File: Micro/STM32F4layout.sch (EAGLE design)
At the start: 38 parts, among them Q1 ASF, U1 LM1085IS-3.3

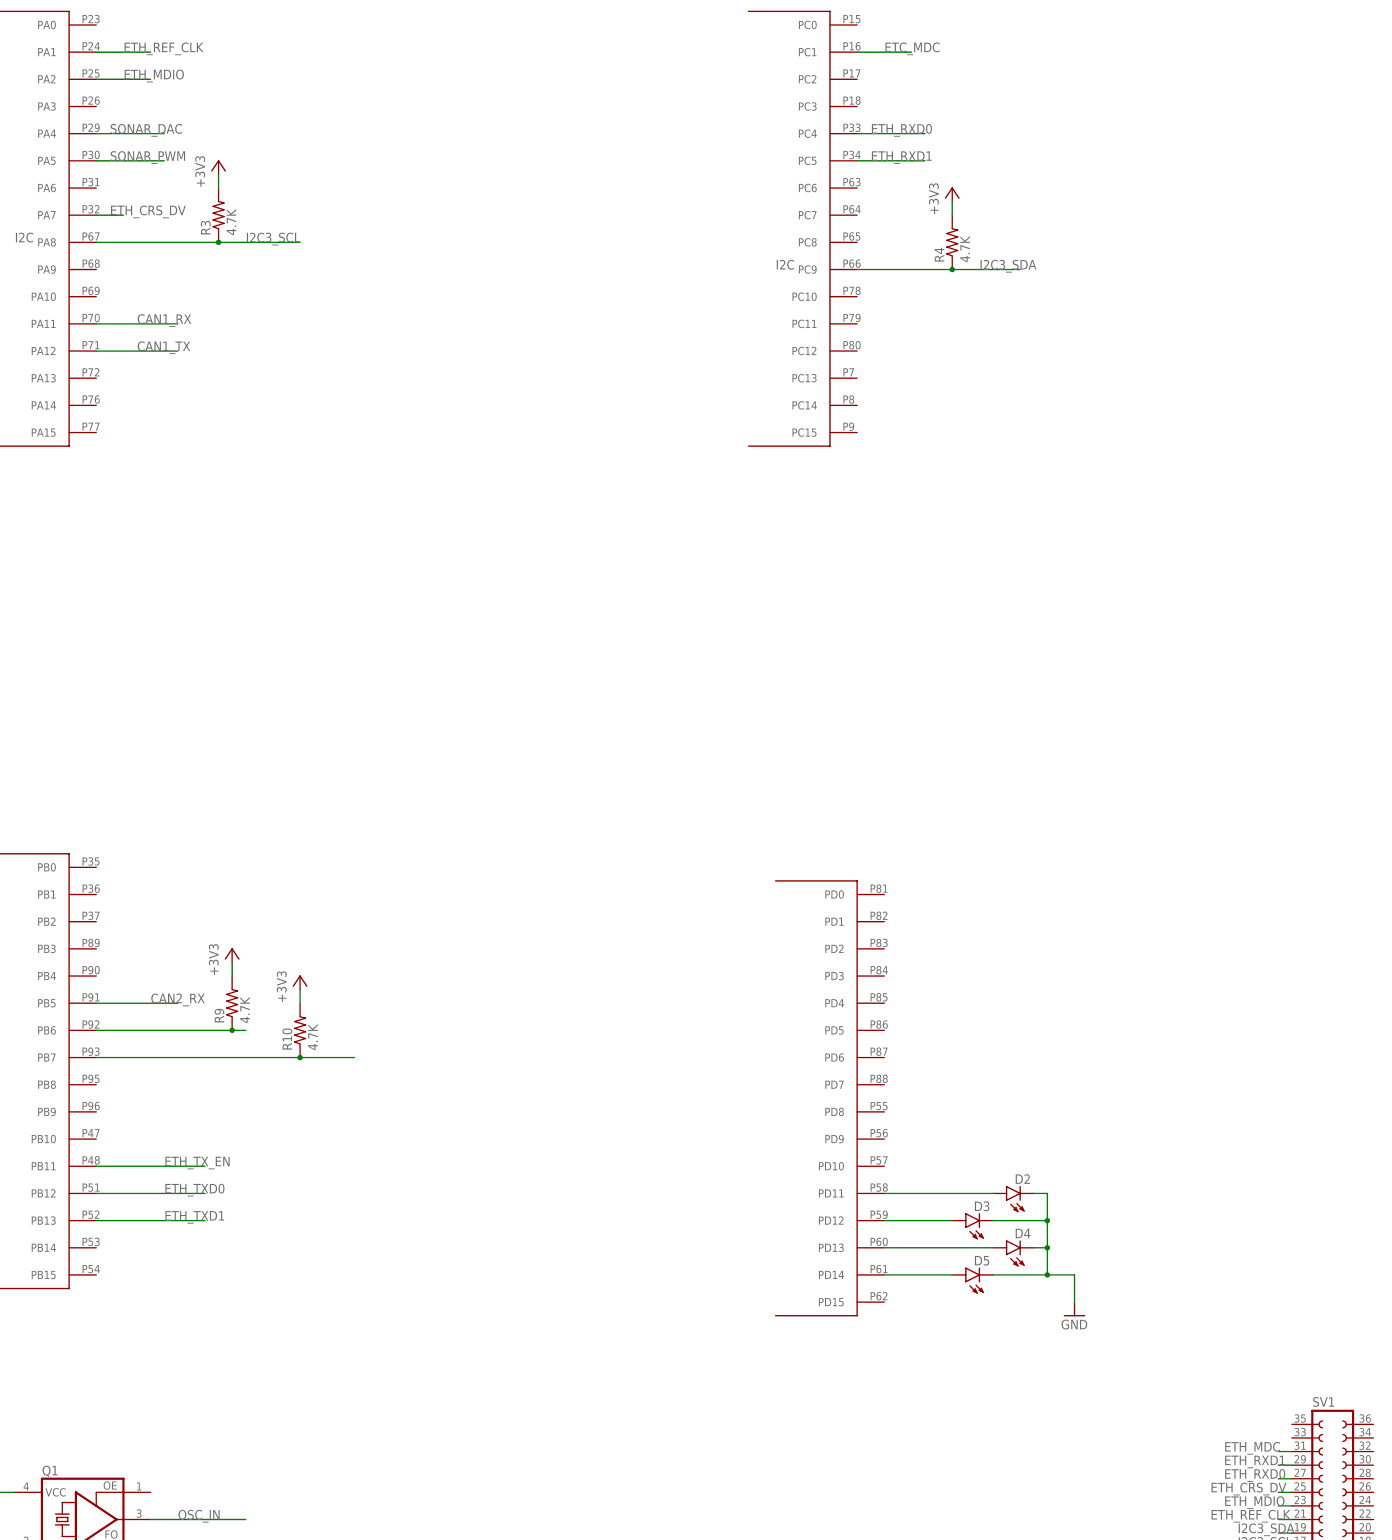
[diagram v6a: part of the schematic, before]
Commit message: Final Version before Design Review
Fixed Pin Out Problems
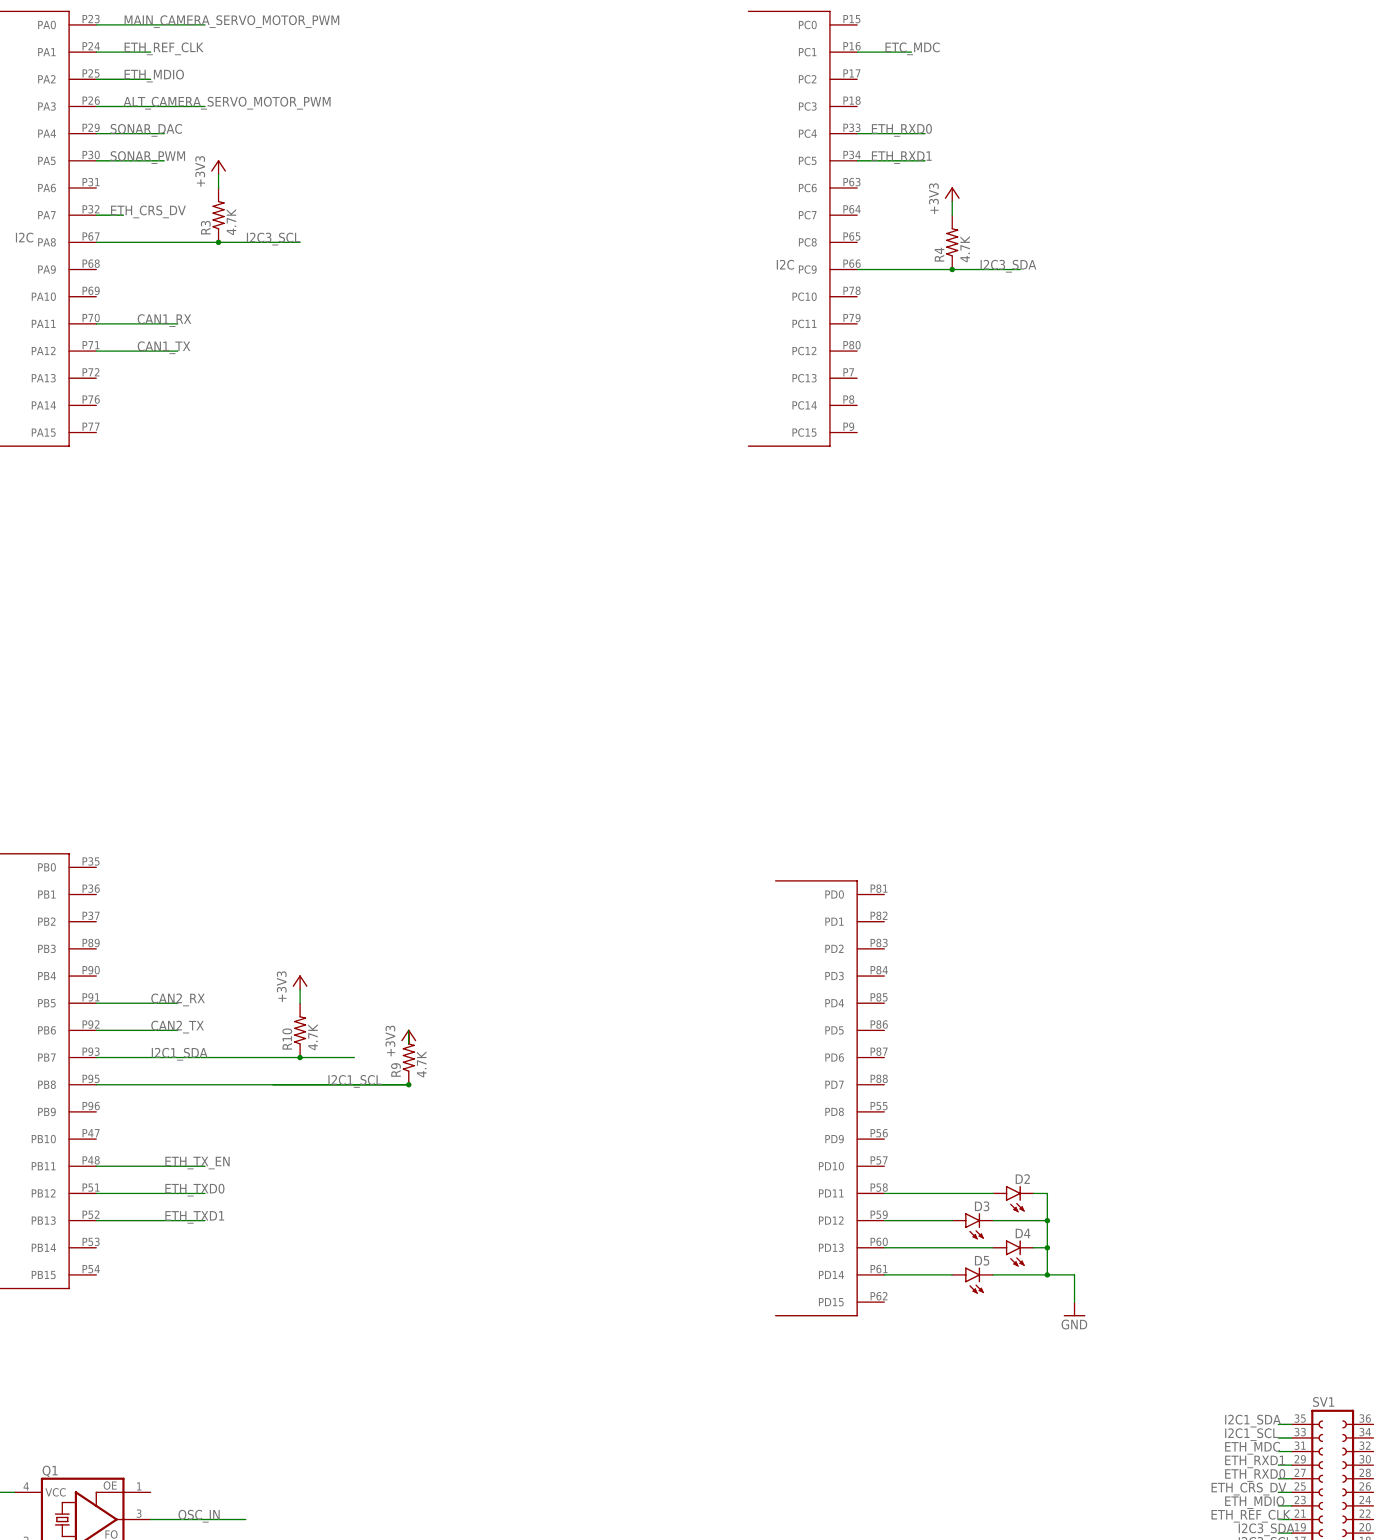
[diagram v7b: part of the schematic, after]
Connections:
- new net ALT_CAMERA_SERVO_MOTOR_PWM: U$1G$1.PA3
- new net MAIN_CAMERA_SERVO_MOTOR_PWM: U$1G$1.PA0
- net CAN2_TX: now also U$1G$2.PB6
- net I2C1_SCL: now also SV1.33, U$1G$2.PB8; no longer U$1G$2.PB6
- net I2C1_SDA: now also SV1.35
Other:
- moved on the sheet: R9
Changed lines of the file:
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@@
 <instance part="GND17" gate="1" x="-439.42" y="-261.62"/>
 <instance part="+3V8" gate="G$1" x="-386.08" y="-226.06"/>
-<instance part="R9" gate="G$1" x="-45.72" y="-63.5" rot="R90"/>
-<instance part="+3V9" gate="G$1" x="-45.72" y="-53.34"/>
+<instance part="R9" gate="G$1" x="-12.7" y="-73.66" rot="R90"/>
+<instance part="+3V9" gate="G$1" x="-12.7" y="-68.58"/>
 <instance part="R10" gate="G$1" x="-33.02" y="-68.58" rot="R90"/>
 <instance part="+3V10" gate="G$1" x="-33.02" y="-58.42"/>
@@
 <pinref part="R9" gate="G$1" pin="2"/>
 <pinref part="+3V9" gate="G$1" pin="+3V3"/>
-<wire x1="-45.72" y1="-55.88" x2="-45.72" y2="-58.42" width="0.1524" layer="91"/>
+<wire x1="-12.7" y1="-71.12" x2="-12.7" y2="-68.58" width="0.1524" layer="91"/>
 </segment>
 <segment>
@@
 <label x="142.24" y="-177.8" size="1.778" layer="95"/>
 </segment>
+<segment>
+<pinref part="U$1" gate="G$2" pin="PB6"/>
+<wire x1="-71.12" y1="-68.58" x2="-55.88" y2="-68.58" width="0.1524" layer="91"/>
+<label x="-60.96" y="-68.58" size="1.778" layer="95"/>
+</segment>
 </net>
 <net name="CAN2_RX" class="0">
@@
 <junction x="-33.02" y="-73.66"/>
 <wire x1="-33.02" y1="-73.66" x2="-22.86" y2="-73.66" width="0.1524" layer="91"/>
+<label x="-60.96" y="-73.66" size="1.778" layer="95"/>
+</segment>
+<segment>
+<pinref part="SV1" gate="G$1" pin="35"/>
+<wire x1="152.4" y1="-142.24" x2="149.86" y2="-142.24" width="0.1524" layer="91"/>
+<label x="139.7" y="-142.24" size="1.778" layer="95"/>
 </segment>
 </net>
 <net name="I2C1_SCL" class="0">
 <segment>
-<pinref part="U$1" gate="G$2" pin="PB6"/>
-<wire x1="-71.12" y1="-68.58" x2="-45.72" y2="-68.58" width="0.1524" layer="91"/>
 <pinref part="R9" gate="G$1" pin="1"/>
-<junction x="-45.72" y="-68.58"/>
-<wire x1="-45.72" y1="-68.58" x2="-43.18" y2="-68.58" width="0.1524" layer="91"/>
-</segment>
-</net>
+<wire x1="-12.7" y1="-78.74" x2="-38.1" y2="-78.74" width="0.1524" layer="91"/>
+<label x="-27.94" y="-78.74" size="1.778" layer="95"/>
+<pinref part="U$1" gate="G$2" pin="PB8"/>
+<wire x1="-12.7" y1="-78.74" x2="-71.12" y2="-78.74" width="0.1524" layer="91"/>
+<junction x="-12.7" y="-78.74"/>
+</segment>
+<segment>
+<pinref part="SV1" gate="G$1" pin="33"/>
+<wire x1="152.4" y1="-144.78" x2="149.86" y2="-144.78" width="0.1524" layer="91"/>
+<label x="139.7" y="-144.78" size="1.778" layer="95"/>
+</segment>
+</net>
+<net name="MAIN_CAMERA_SERVO_MOTOR_PWM" class="0">
+<segment>
+<pinref part="U$1" gate="G$1" pin="PA0"/>
+<wire x1="-71.12" y1="119.38" x2="-50.8" y2="119.38" width="0.1524" layer="91"/>
+<label x="-66.04" y="119.38" size="1.778" layer="95"/>
+</segment>
+</net>
+<net name="ALT_CAMERA_SERVO_MOTOR_PWM" class="0">
+<segment>
+<pinref part="U$1" gate="G$1" pin="PA3"/>
+<wire x1="-71.12" y1="104.14" x2="-50.8" y2="104.14" width="0.1524" layer="91"/>
+<label x="-66.04" y="104.14" size="1.778" layer="95"/>
+</segment>
+</net>
